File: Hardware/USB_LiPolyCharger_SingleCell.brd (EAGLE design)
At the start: 31.8 x 33 mm, 25 parts, among them J1 POWER_JACKPTH_LOCK, U1 MCP73831, X1 USBSMD

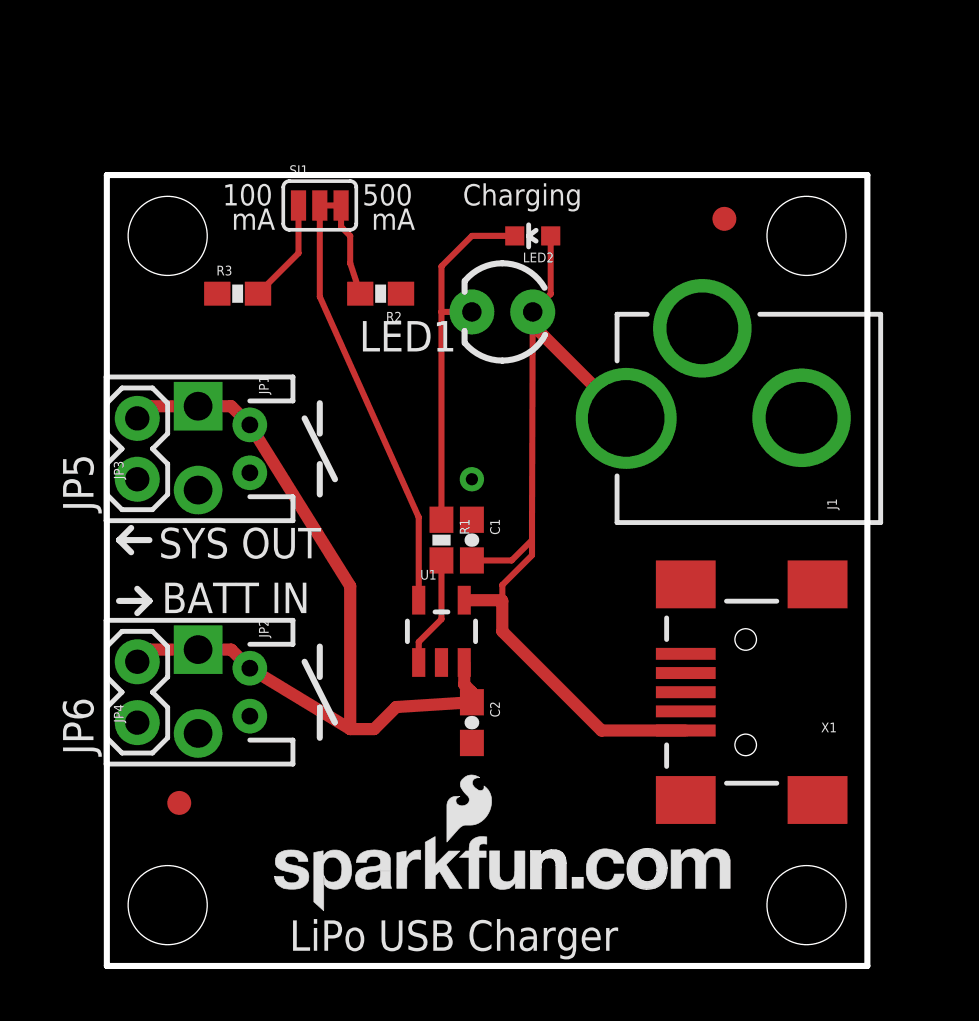
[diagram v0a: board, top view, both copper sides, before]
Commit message: Added Diodes/Prog RES
Added 2x MBRA diodes to the power lines of the USB and Barrel jack .
Also added an optional PTH res for the PROG line.
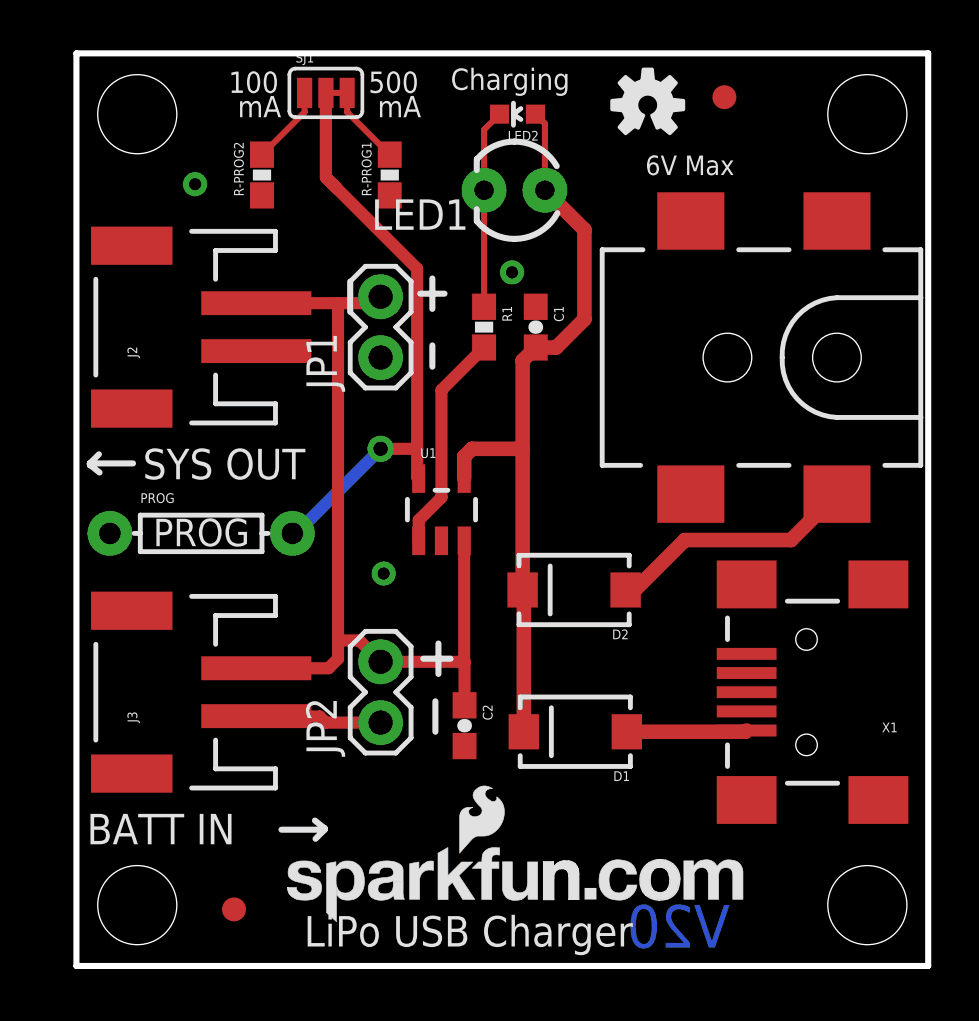
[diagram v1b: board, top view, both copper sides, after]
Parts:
- removed JP3, JP4: JST, SparkFun:JST-2-PTH
- removed JP5, JP6: M02, SparkFun:1X02
- removed R2: 2k, SparkFun:0603-RES
- removed R3: 10k, SparkFun:0603-RES
- removed U$: CREATIVE_COMMONS, SparkFun:CREATIVE_COMMONS
- added D1, D2: MBRA140, SparkFun-DiscreteSemi:SMA-DIODE
- added FRAME1: FRAME-LETTER, SparkFun-Aesthetics:CREATIVE_COMMONS
- added J2, J3: (no value), SparkFun-Connectors:JST-2-SMD
- added LOGO1: OSHW-LOGOS, SparkFun-Aesthetics:OSHW-LOGO-S
- added PROG: (no value), SparkFun-Resistors:AXIAL-0.3
- added R-PROG1: 2k, SparkFun-Resistors:0603-RES
- added R-PROG2: 10k, SparkFun-Resistors:0603-RES
- C1, C2: device SparkFun:0603-CAP -> SparkFun-Capacitors:0603-CAP
- J1: value POWER_JACKPTH_LOCK -> POWER_JACKSMD; device SparkFun:POWER_JACK_PTH_LOCK -> SparkFun-Connectors:POWER_JACK_SMD
- JP1, JP2: value SCREW -> M02PTH; device SparkFun:SCREWTERMINAL-3.5MM-2-NS -> SparkFun-Connectors:1X02
- LED2: device SparkFun:LED-0603 -> SparkFun-LED:LED-0603
- R1: device SparkFun:0603-RES -> SparkFun-Resistors:0603-RES
- U1: device SparkFun:SOT23-5 -> SparkFun-PowerIC:SOT23-5
- X1: device SparkFun:USB-MINIB -> SparkFun-Connectors:USB-MINIB
- moved C1 9.28 mm to (17.9, 26.7)
- moved R1 9.07 mm to (15.7, 26.7)
- moved JP2 8.21 mm to (11.4, 10.2), turned to 90 degrees
- moved JP1 7.89 mm to (11.4, 25.4), turned to 90 degrees
- moved J1 5.68 mm to (30.5, 25.4), turned to 180 degrees
- moved JP10 5.68 mm to (31.8, 35.6)
- moved JP8 5.24 mm to (1.27, 35.6)
- moved LED2 5.12 mm to (17.1, 35.6)
- moved LED1 5.11 mm to (17.0, 32.4)
- moved JP13 5.08 mm to (25.8, 36.3)
- moved U1 5.08 mm to (14.0, 19.1)
- moved JP12 5.00 mm to (5.31, 2.36)
- moved SJ1 4.71 mm to (9.14, 36.4)
- moved JP7 2.54 mm to (31.8, 2.54)
- moved X1 2.54 mm to (29.2, 11.4)
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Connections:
- removed net VBAT: C2.1, JP1.1, JP2.1, JP3.2, JP4.2, JP5.2, JP6.2, U1.3
- new net N$10: C2.1, J2.2, J3.2, JP1.2, JP2.2, U1.3
- new net N$6: D1.A, X1.VBUS
- new net N$8: D2.A, J1.VIN0
- net GND: now also J1.P$4, J2.1, J3.1, JP1.1, JP2.1, PROG.P$1, R-PROG1.1, R-PROG2.1; no longer J1.GNDBREAK, JP1.2, JP2.2, JP3.1, JP4.1, JP5.1, JP6.1, R2.1, R3.1
- net N$1: now also D1.C, D2.C; no longer J1.PWR, X1.VBUS
- net N$4: now also R-PROG1.2; no longer R2.2
- net N$7: now also R-PROG2.2; no longer R3.2
- net PROG: now also PROG.P$2
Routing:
- net VBAT: track 36.5 -> 0.00 mm
- net N$10: track 0.00 -> 36.2 mm
- net N$8: track 0.00 -> 10.5 mm
- net PROG: track 17.4 -> 24.9 mm, vias 0 -> 1
- net N$3: track 15.4 -> 8.31 mm
- net N$1: track 37.2 -> 32.0 mm
- net N$6: track 0.00 -> 5.02 mm
- net N$2: track 4.65 -> 9.20 mm
- net GND: track 0.00 -> 3.97 mm, vias 1 -> 3
- net N$7: track 4.38 -> 3.32 mm
- net N$4: track 3.96 -> 3.37 mm
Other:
- board size 31.8 x 33 mm -> 35.6 x 38.1 mm
- board text added: "6V Max"
- board text added: "Jim Lidblom"
- board text added: "PROG"
- board text added: "Revised by: Patrick Alberts"
- board text added: "V20"
